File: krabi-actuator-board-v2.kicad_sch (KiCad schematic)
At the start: 22 parts, among them J1 Power, J2 PWM, J3 Analog, J4 PWM, J5 Analog, J6 Communication, J7 Digital, J8 Conn_01x02_Pin, U1 XGZP6897D_differential_pressu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, U2 XGZP6897D_differential_pressu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

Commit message: Full command of the servos 6V power
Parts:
- added CFF_VR1, CFF_VR2: 3.3nF, symbol Device:C
- added Cin_VR1, Cin_VR2: 470µF, Capacitor_THT:CP_Radial_D5.0mm_P2.00mm, symbol Device:C_Polarized
- added Cout_VR1, Cout_VR2: 470µF, symbol Device:C
- added D1_VR1, D1_VR2: 20V 5A, Diode_SMD:D_0805_2012Metric, symbol Device:D_Schottky
- added L1_VR1, L1_VR2: 33µH, symbol Device:L
- added R1_VR1, R1_VR2: 38.8k, Resistor_SMD:R_0805_2012Metric, symbol Device:R
- added R2_VR1, R2_VR2: 10k, Resistor_SMD:R_0805_2012Metric, symbol Device:R
- added RB_ON_OFF_ALIM1: 6.65k, Resistor_SMD:R_0805_2012Metric, symbol Device:R
- added RPU_ON_OFF_ALIM1, RT_ON_OFF_ALIM1: 20k, Resistor_SMD:R_0805_2012Metric, symbol Device:R
- added VR1, VR2: LM2596s, symbol Krabi:LM2596s
- C1: value 10mF -> 1mF; footprint Capacitor_THT:CP_Radial_D10.0mm_P5.00mm -> Capacitor_THT:CP_Radial_D5.0mm_P2.00mm
- U1, U2, U3, U4: footprint LibraryVictor:SOIC-8_7.5x5.85mm_P1.27mm -> Krabi:SOIC-8-11mmx7mm outside pad 1.9
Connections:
- net 12_V: now also Cin_VR1.1, Cin_VR2.1, RT_ON_OFF_ALIM1.1, VR1.1 (Vin), VR2.1 (Vin)
- net GND: now also Cin_VR1.2, Cin_VR2.2, Cout_VR1.2, Cout_VR2.2, D1_VR1.2 (A), D1_VR2.2 (A), R2_VR1.2, R2_VR2.2, RB_ON_OFF_ALIM1.2, VR1.3 (GND), VR2.3 (GND)
- net 23 renamed ON/OFF
- net ON/OFF: now also RPU_ON_OFF_ALIM1.2, VR1.5 (ON/OFF), VR2.5 (ON/OFF)
- new net: RB_ON_OFF_ALIM1.1, RPU_ON_OFF_ALIM1.1, RT_ON_OFF_ALIM1.2
- new net: CFF_VR2.1, D1_VR2.1 (K), L1_VR2.1, R1_VR2.1, VR2.2 (Ouput)
- new net: CFF_VR2.2, R1_VR2.2, R2_VR2.1, VR2.4 (Feedback)
- new net: CFF_VR1.1, D1_VR1.1 (K), L1_VR1.1, R1_VR1.1, VR1.2 (Ouput)
- new net: CFF_VR1.2, R1_VR1.2, R2_VR1.1, VR1.4 (Feedback)
- new net 6V1: Cout_VR1.1, L1_VR1.2
- new net 6V2: Cout_VR2.1, L1_VR2.2

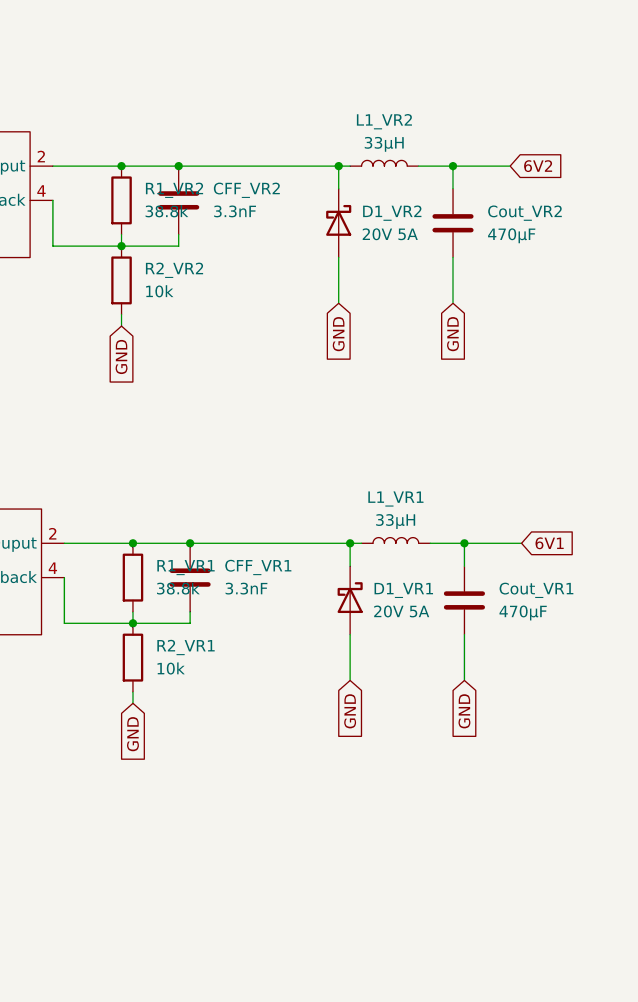
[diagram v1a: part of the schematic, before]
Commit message: Add Power ON leds
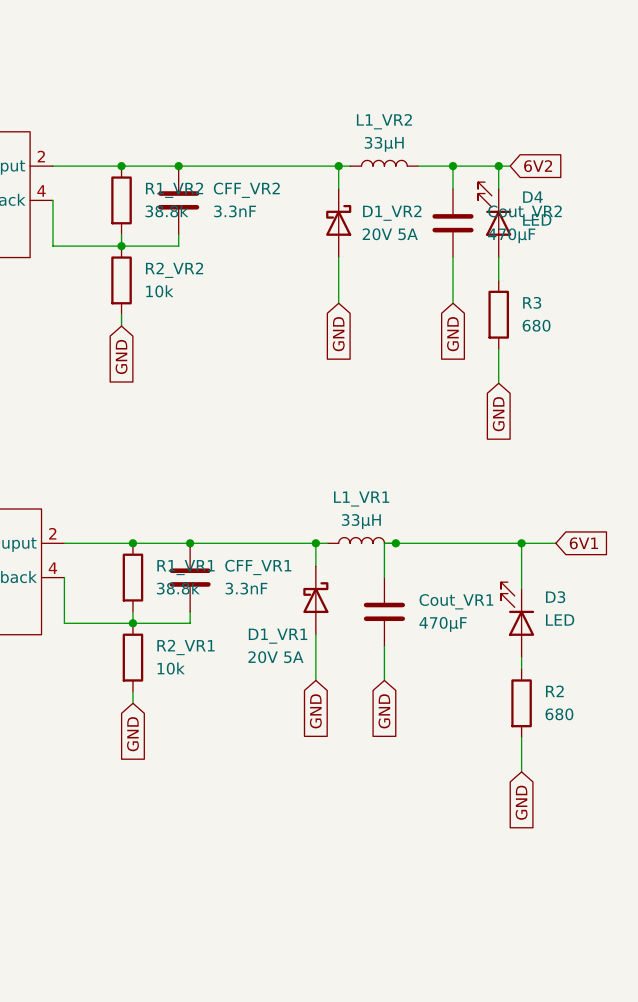
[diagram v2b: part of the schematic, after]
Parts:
- added D3, D4: LED, LED_SMD:LED_0805_2012Metric, symbol Device:LED
- added R2, R3: 680, Resistor_SMD:R_0805_2012Metric, symbol Device:R
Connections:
- net 6V1: now also D3.1 (K)
- net 6V2: now also D4.1 (K)
- net GND: now also R2.2, R3.2
- new net: D4.2 (A), R3.1
- new net: D3.2 (A), R2.1
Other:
- moved on the sheet: Cout_VR1, D1_VR1, L1_VR1

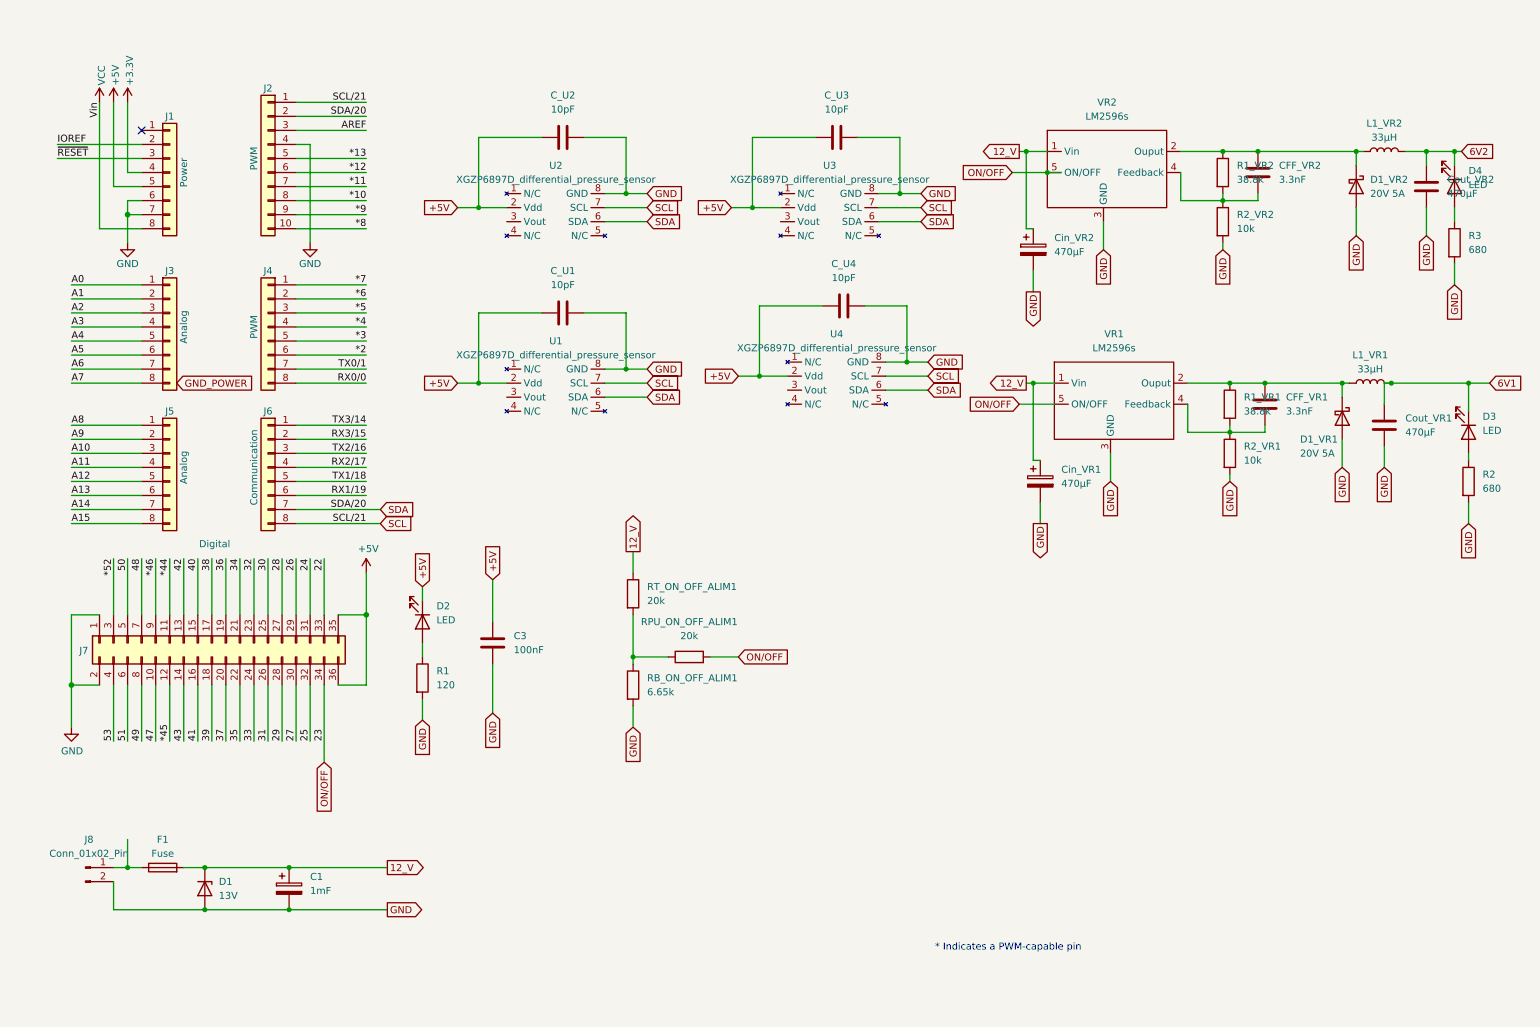
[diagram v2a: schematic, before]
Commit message: Servos are connecteds
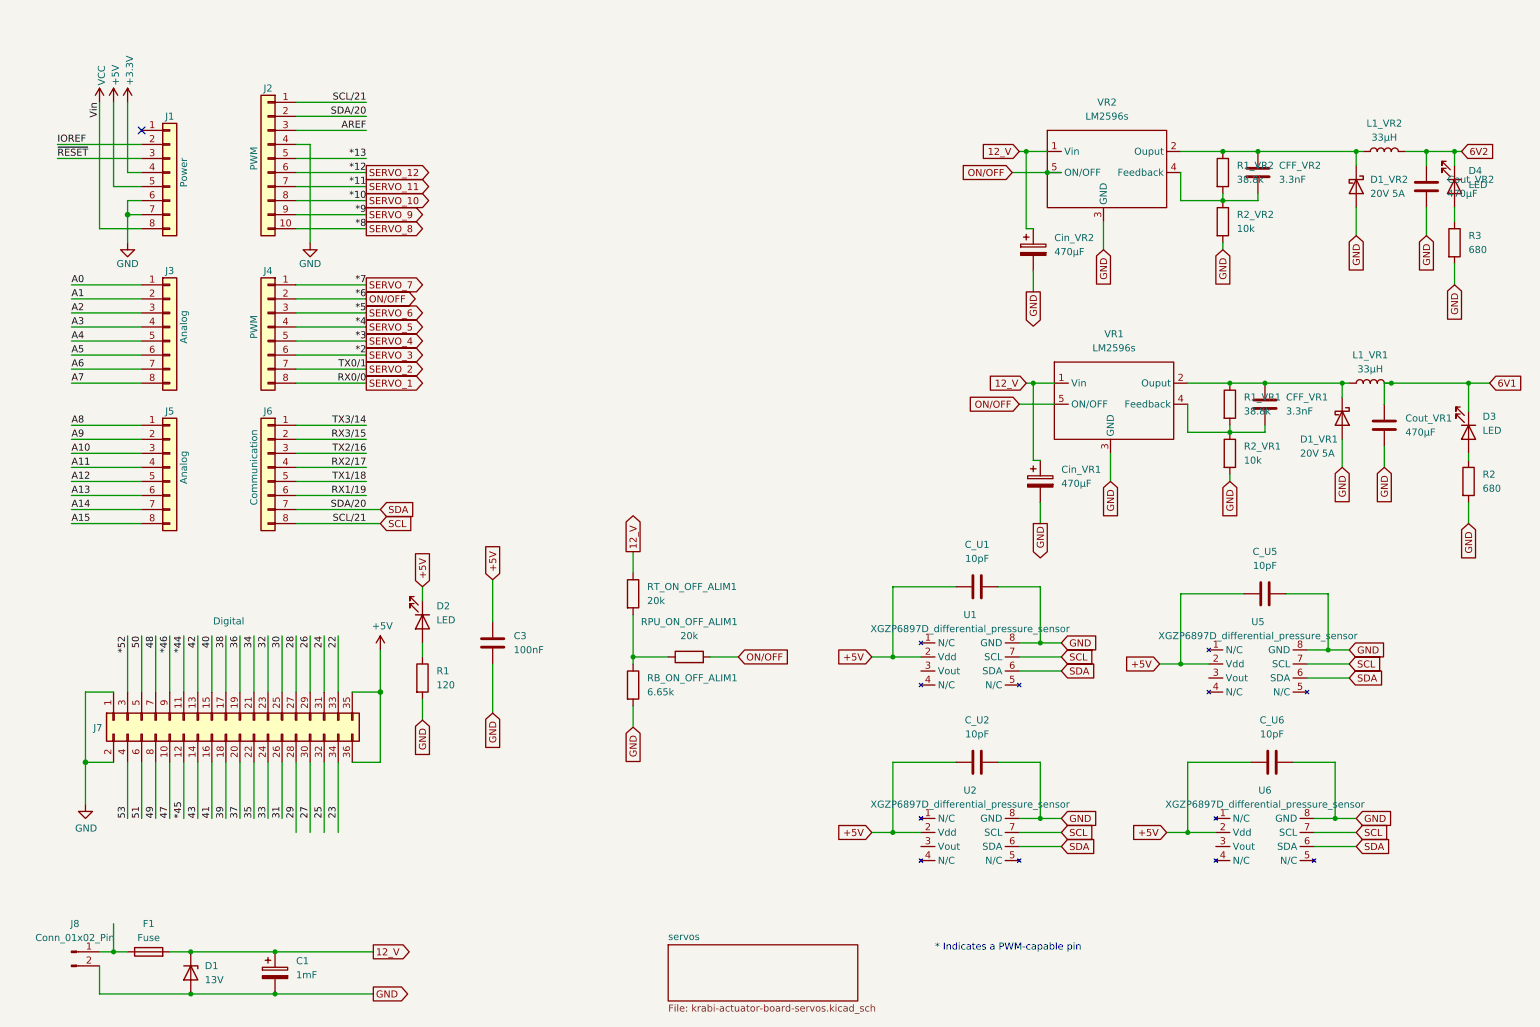
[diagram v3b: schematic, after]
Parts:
- removed C_U3, C_U4: 10pF, Capacitor_SMD:C_0805_2012Metric, symbol Device:C
- removed U3, U4: XGZP6897D_differential_pressure_sensor, Krabi:SOIC-8-11mmx7mm outside pad 1.9, symbol Krabi:XGZP6897D_differential_pressure_sensor
- added C_U5, C_U6: 10pF, Capacitor_SMD:C_0805_2012Metric, symbol Device:C
- added U5, U6: XGZP6897D_differential_pressure_sensor, Krabi:SOIC-8-11mmx7mm outside pad 1.9, symbol Krabi:XGZP6897D_differential_pressure_sensor
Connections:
- net *6 is gone; now on net ON/OFF: J4.2 (Pin_2)
- net +5V: now also C_U5.1, C_U6.1, U5.2 (Vdd), U6.2 (Vdd)
- net GND: now also C_U5.2, C_U6.2, U5.8 (GND), U6.8 (GND)
- net ON/OFF: no longer J7.34 (Pin_34)
- net SCL: now also U5.7 (SCL), U6.7 (SCL)
- net SDA: now also U5.6 (SDA), U6.6 (SDA)
- net *10 renamed SERVO_10
- net *11 renamed SERVO_11
- net *12 renamed SERVO_12
- net *2 renamed SERVO_3
- net *3 renamed SERVO_4
- net *4 renamed SERVO_5
- net *5 renamed SERVO_6
- net *7 renamed SERVO_7
- net *8 renamed SERVO_8
- net *9 renamed SERVO_9
- net RX0/0 renamed SERVO_1
- net TX0/1 renamed SERVO_2
- new net 23: J7.34 (Pin_34)
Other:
- added sheet servos (krabi-actuator-board-servos.kicad_sch)
- moved on the sheet: C1, D1, F1, J7, J8

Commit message: Add Vaccum pump output and control
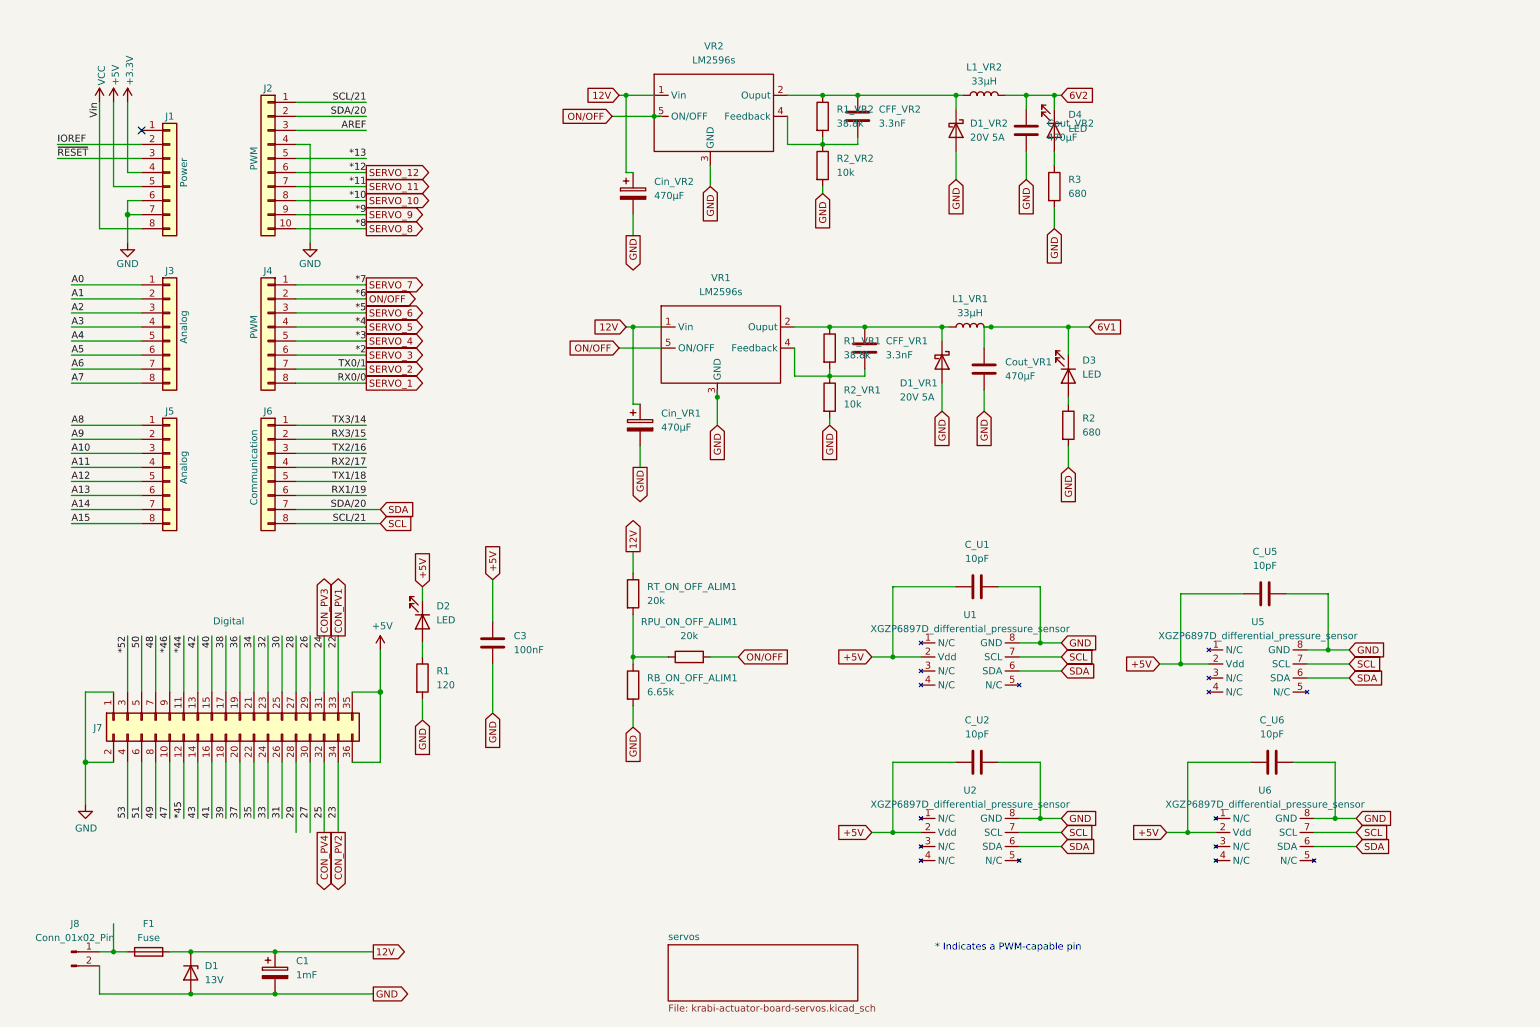
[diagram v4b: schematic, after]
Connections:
- net 12_V renamed 12V
- net 22 renamed CON_PV1
- net 23 renamed CON_PV2
- net 24 renamed CON_PV3
- net 25 renamed CON_PV4
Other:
- moved on the sheet: CFF_VR1, CFF_VR2, Cin_VR1, Cin_VR2, Cout_VR1, Cout_VR2, D1_VR1, D1_VR2, D3, D4, L1_VR1, L1_VR2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

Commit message: Measure the current of the Power supplies
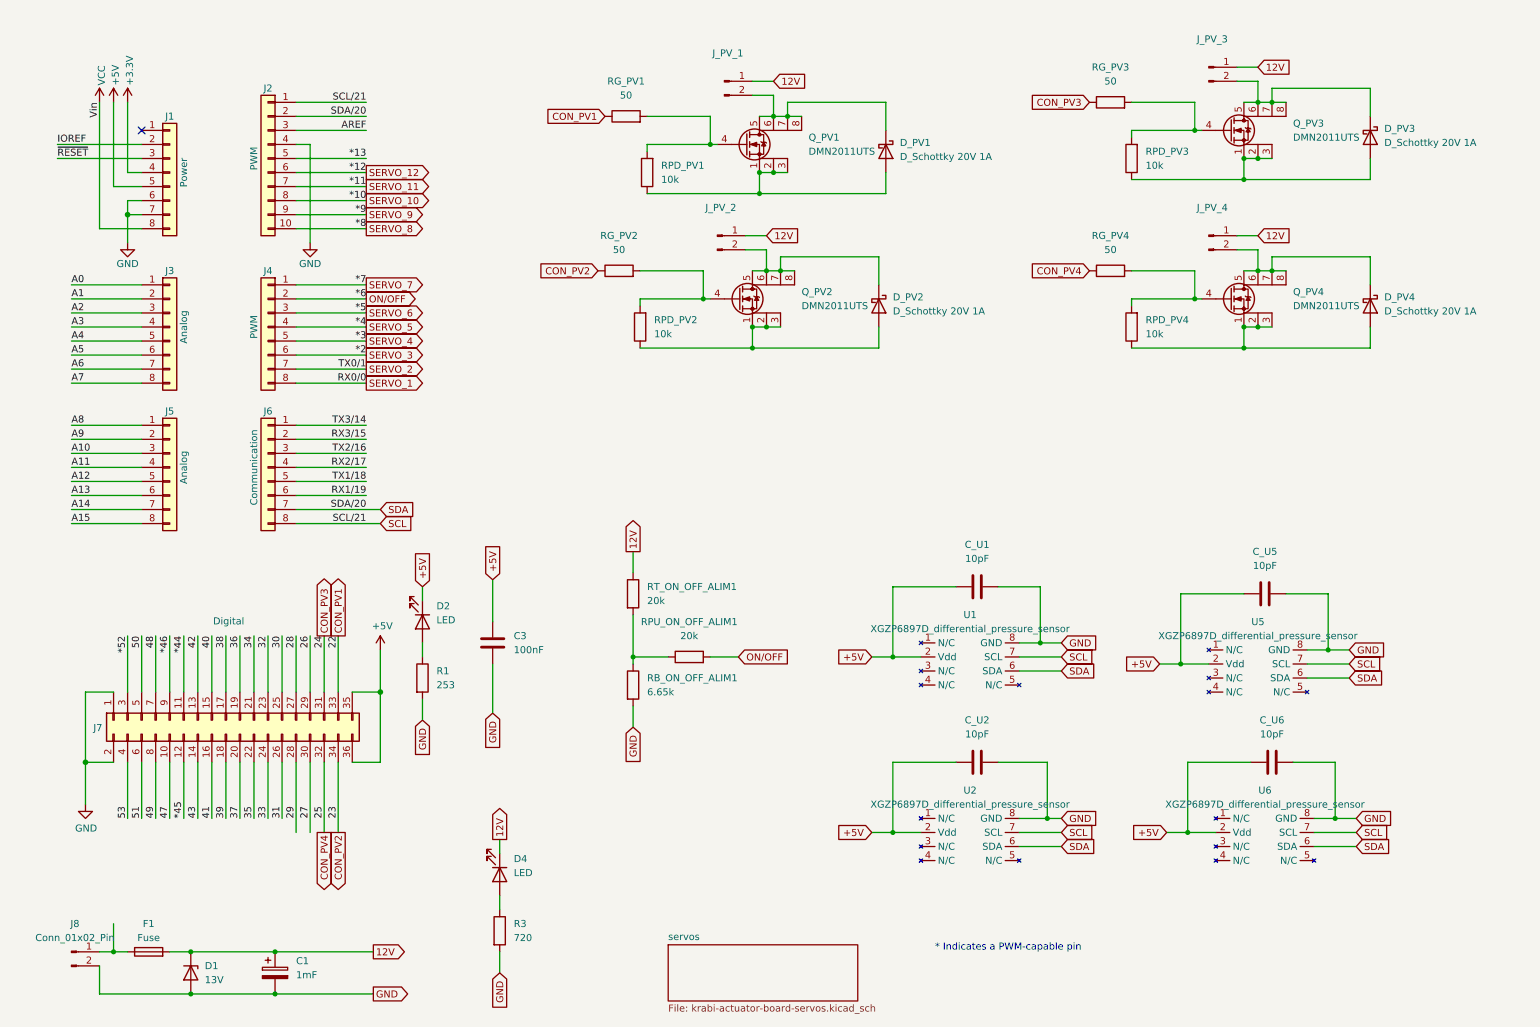
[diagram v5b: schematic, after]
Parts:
- removed CFF_VR1, CFF_VR2: 3.3nF, symbol Device:C
- removed Cin_VR1, Cin_VR2: 470µF, Capacitor_THT:CP_Radial_D5.0mm_P2.00mm, symbol Device:C_Polarized
- removed Cout_VR1, Cout_VR2: 470µF, symbol Device:C
- removed D1_VR1, D1_VR2: 20V 5A, Diode_SMD:D_0805_2012Metric, symbol Device:D_Schottky
- removed D3: LED, LED_SMD:LED_0805_2012Metric, symbol Device:LED
- removed L1_VR1, L1_VR2: 33µH, symbol Device:L
- removed R1_VR1, R1_VR2: 38.8k, Resistor_SMD:R_0805_2012Metric, symbol Device:R
- removed R2: 680, Resistor_SMD:R_0805_2012Metric, symbol Device:R
- removed R2_VR1, R2_VR2: 10k, Resistor_SMD:R_0805_2012Metric, symbol Device:R
- removed VR1, VR2: LM2596s, symbol Krabi:LM2596s
- added D_PV1, D_PV2, D_PV3, D_PV4: D_Schottky 20V 1A, symbol Device:D_Schottky
- added J_PV_1, J_PV_2, J_PV_3, J_PV_4: ~, symbol Connector:Conn_01x02_Pin
- added Q_PV1, Q_PV2, Q_PV3, Q_PV4: DMN2011UTS, Package_SO:TSSOP-8_4.4x3mm_P0.65mm, symbol Krabi:DMN2011UTS
- added RG_PV1, RG_PV2, RG_PV3, RG_PV4: 50, symbol Device:R
- added RPD_PV1, RPD_PV2, RPD_PV3, RPD_PV4: 10k, symbol Device:R
- R1: value 120 -> 253
- R3: value 680 -> 720
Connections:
- net 6V2 is gone; now on net 12V: D4.1 (K)
- net 12V: now also J_PV_1.1 (Pin_1), J_PV_2.1 (Pin_1), J_PV_3.1 (Pin_1), J_PV_4.1 (Pin_1)
- net CON_PV1: now also RG_PV1.1
- net CON_PV2: now also RG_PV2.1
- net CON_PV3: now also RG_PV3.1
- net CON_PV4: now also RG_PV4.1
- new net: D_PV3.2 (A), Q_PV3.1 (S), Q_PV3.2 (S), Q_PV3.3 (S), RPD_PV3.1
- new net: Q_PV3.4 (G), RG_PV3.2, RPD_PV3.2
- new net: D_PV3.1 (K), J_PV_3.2 (Pin_2), Q_PV3.5 (D), Q_PV3.6 (D), Q_PV3.7 (D), Q_PV3.8 (D)
- new net: D_PV4.2 (A), Q_PV4.1 (S), Q_PV4.2 (S), Q_PV4.3 (S), RPD_PV4.1
- new net: Q_PV4.4 (G), RG_PV4.2, RPD_PV4.2
- new net: D_PV4.1 (K), J_PV_4.2 (Pin_2), Q_PV4.5 (D), Q_PV4.6 (D), Q_PV4.7 (D), Q_PV4.8 (D)
- new net: Q_PV1.4 (G), RG_PV1.2, RPD_PV1.2
- new net: D_PV2.2 (A), Q_PV2.1 (S), Q_PV2.2 (S), Q_PV2.3 (S), RPD_PV2.1
- new net: Q_PV2.4 (G), RG_PV2.2, RPD_PV2.2
- new net: D_PV2.1 (K), J_PV_2.2 (Pin_2), Q_PV2.5 (D), Q_PV2.6 (D), Q_PV2.7 (D), Q_PV2.8 (D)
- new net: D_PV1.2 (A), Q_PV1.1 (S), Q_PV1.2 (S), Q_PV1.3 (S), RPD_PV1.1
- new net: D_PV1.1 (K), J_PV_1.2 (Pin_2), Q_PV1.5 (D), Q_PV1.6 (D), Q_PV1.7 (D), Q_PV1.8 (D)

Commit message: Update servo with capa & add led strip page
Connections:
- net A0 renamed CURRENT_VR2
- net A1 renamed CURRENT_VR1
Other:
- added sheet LEDstrip (krabi-actuator-board-v2-ledstrip.kicad_sch)
- moved on the sheet: J1, J2, J3, J4, J5, J6
